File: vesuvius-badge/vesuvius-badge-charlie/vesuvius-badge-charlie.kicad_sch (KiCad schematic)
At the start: 9 parts, among them U1 IS31FL3731-QF, U2 Pico

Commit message: letters and vesuvius
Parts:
- added D1, D10, D100, D101, D102, D103, D104, D105, D106, D107, D108, D109, D11, D110, D111, D112, D113, D114, D115, D116, D117, D118, D119, D12, D120, D121, D122, D123, D124, D125, D126, D127, D128, D129, D13, D130, D131, D132, D133, D134, D135, D136, D137, D138, D139, D14, D140, D141, D142, D143, D144, D15, D16, D17, D18, D19, D2, D20, D21, D22, D23, D24, D25, D26, D27, D28, D29, D3, D30, D31, D32, D33, D34, D35, D36, D37, D38, D39, D4, D40, D41, D42, D43, D44, D45, D46, D47, D48, D49, D5, D50, D51, D52, D53, D54, D55, D56, D57, D58, D59, D6, D60, D61, D62, D63, D64, D65, D66, D67, D68, D69, D7, D70, D71, D72, D73, D74, D75, D76, D77, D78, D79, D8, D80, D81, D82, D83, D84, D85, D86, D87, D88, D89, D9, D90, D91, D92, D93, D94, D95, D96, D97, D98, D99: LED, LED_SMD:LED_0402_1005Metric, symbol Device:LED
- C1, C2, C3: renamed from C?; footprint (none) -> Capacitor_SMD:C_0603_1608Metric
- R1, R2, R3, R4: renamed from R?; footprint (none) -> Resistor_SMD:R_0603_1608Metric
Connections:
- net CA9: now reaches U1.1 (CA9)
- net CA9: now also D104.2 (A), D120.2 (A), D129.1 (K), D130.1 (K), D131.1 (K), D132.1 (K), D133.1 (K), D134.1 (K), D135.1 (K), D136.1 (K), D24.2 (A), D40.2 (A), D56.2 (A), D72.2 (A), D8.2 (A), D88.2 (A)
- net CB4: now reaches U1.10 (CB4)
- net CB4: now also D108.2 (A), D11.2 (A), D124.2 (A), D140.2 (A), D27.2 (A), D43.2 (A), D57.1 (K), D58.1 (K), D59.1 (K), D60.1 (K), D61.1 (K), D62.1 (K), D63.1 (K), D64.1 (K), D76.2 (A), D92.2 (A)
- net CB5: now reaches U1.11 (CB5)
- net CB5: now also D109.2 (A), D12.2 (A), D125.2 (A), D141.2 (A), D28.2 (A), D44.2 (A), D60.2 (A), D73.1 (K), D74.1 (K), D75.1 (K), D76.1 (K), D77.1 (K), D78.1 (K), D79.1 (K), D80.1 (K), D93.2 (A)
- net CB6: now reaches U1.12 (CB6)
- net CB6: now also D110.2 (A), D126.2 (A), D13.2 (A), D142.2 (A), D29.2 (A), D45.2 (A), D61.2 (A), D77.2 (A), D89.1 (K), D90.1 (K), D91.1 (K), D92.1 (K), D93.1 (K), D94.1 (K), D95.1 (K), D96.1 (K)
- net CB7: now reaches U1.13 (CB7)
- net CB7: now also D105.1 (K), D106.1 (K), D107.1 (K), D108.1 (K), D109.1 (K), D110.1 (K), D111.1 (K), D112.1 (K), D127.2 (A), D14.2 (A), D143.2 (A), D30.2 (A), D46.2 (A), D62.2 (A), D78.2 (A), D94.2 (A)
- net CB8: now reaches U1.14 (CB8)
- net CB8: now also D111.2 (A), D121.1 (K), D122.1 (K), D123.1 (K), D124.1 (K), D125.1 (K), D126.1 (K), D127.1 (K), D128.1 (K), D144.2 (A), D15.2 (A), D31.2 (A), D47.2 (A), D63.2 (A), D79.2 (A), D95.2 (A)
- net CB9: now reaches U1.15 (CB9)
- net CB9: now also D112.2 (A), D128.2 (A), D137.1 (K), D138.1 (K), D139.1 (K), D140.1 (K), D141.1 (K), D142.1 (K), D143.1 (K), D144.1 (K), D16.2 (A), D32.2 (A), D48.2 (A), D64.2 (A), D80.2 (A), D96.2 (A)
- net CA1: now reaches U1.21 (CA1)
- net CA1: now also D1.1 (K), D113.2 (A), D129.2 (A), D17.2 (A), D2.1 (K), D3.1 (K), D33.2 (A), D4.1 (K), D49.2 (A), D5.1 (K), D6.1 (K), D65.2 (A), D7.1 (K), D8.1 (K), D81.2 (A), D97.2 (A)
- net CA2: now reaches U1.22 (CA2)
- net CA2: now also D1.2 (A), D114.2 (A), D130.2 (A), D17.1 (K), D18.1 (K), D19.1 (K), D20.1 (K), D21.1 (K), D22.1 (K), D23.1 (K), D24.1 (K), D34.2 (A), D50.2 (A), D66.2 (A), D82.2 (A), D98.2 (A)
- net CA3: now reaches U1.23 (CA3)
- net CA3: now also D115.2 (A), D131.2 (A), D18.2 (A), D2.2 (A), D33.1 (K), D34.1 (K), D35.1 (K), D36.1 (K), D37.1 (K), D38.1 (K), D39.1 (K), D40.1 (K), D51.2 (A), D67.2 (A), D83.2 (A), D99.2 (A)
- net CA4: now reaches U1.24 (CA4)
- net CA4: now also D100.2 (A), D116.2 (A), D132.2 (A), D19.2 (A), D3.2 (A), D35.2 (A), D49.1 (K), D50.1 (K), D51.1 (K), D52.1 (K), D53.1 (K), D54.1 (K), D55.1 (K), D56.1 (K), D68.2 (A), D84.2 (A)
- net CA5: now reaches U1.25 (CA5)
- net CA5: now also D101.2 (A), D117.2 (A), D133.2 (A), D20.2 (A), D36.2 (A), D4.2 (A), D52.2 (A), D65.1 (K), D66.1 (K), D67.1 (K), D68.1 (K), D69.1 (K), D70.1 (K), D71.1 (K), D72.1 (K), D85.2 (A)
- net CA6: now reaches U1.26 (CA6)
- net CA6: now also D102.2 (A), D118.2 (A), D134.2 (A), D21.2 (A), D37.2 (A), D5.2 (A), D53.2 (A), D69.2 (A), D81.1 (K), D82.1 (K), D83.1 (K), D84.1 (K), D85.1 (K), D86.1 (K), D87.1 (K), D88.1 (K)
- net CA7: now reaches U1.27 (CA7)
- net CA7: now also D100.1 (K), D101.1 (K), D102.1 (K), D103.1 (K), D104.1 (K), D119.2 (A), D135.2 (A), D22.2 (A), D38.2 (A), D54.2 (A), D6.2 (A), D70.2 (A), D86.2 (A), D97.1 (K), D98.1 (K), D99.1 (K)
- net CA8: now reaches U1.28 (CA8)
- net CA8: now also D103.2 (A), D113.1 (K), D114.1 (K), D115.1 (K), D116.1 (K), D117.1 (K), D118.1 (K), D119.1 (K), D120.1 (K), D136.2 (A), D23.2 (A), D39.2 (A), D55.2 (A), D7.2 (A), D71.2 (A), D87.2 (A)
- net CB1: now reaches U1.7 (CB1)
- net CB1: now also D10.1 (K), D105.2 (A), D11.1 (K), D12.1 (K), D121.2 (A), D13.1 (K), D137.2 (A), D14.1 (K), D15.1 (K), D16.1 (K), D25.2 (A), D41.2 (A), D57.2 (A), D73.2 (A), D89.2 (A), D9.1 (K)
- net CB2: now reaches U1.8 (CB2)
- net CB2: now also D106.2 (A), D122.2 (A), D138.2 (A), D25.1 (K), D26.1 (K), D27.1 (K), D28.1 (K), D29.1 (K), D30.1 (K), D31.1 (K), D32.1 (K), D42.2 (A), D58.2 (A), D74.2 (A), D9.2 (A), D90.2 (A)
- net CB3: now reaches U1.9 (CB3)
- net CB3: now also D10.2 (A), D107.2 (A), D123.2 (A), D139.2 (A), D26.2 (A), D41.1 (K), D42.1 (K), D43.1 (K), D44.1 (K), D45.1 (K), D46.1 (K), D47.1 (K), D48.1 (K), D59.2 (A), D75.2 (A), D91.2 (A)
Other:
- moved on the sheet: C1, C2, C3, R1, R2, R3, R4, U1, U2

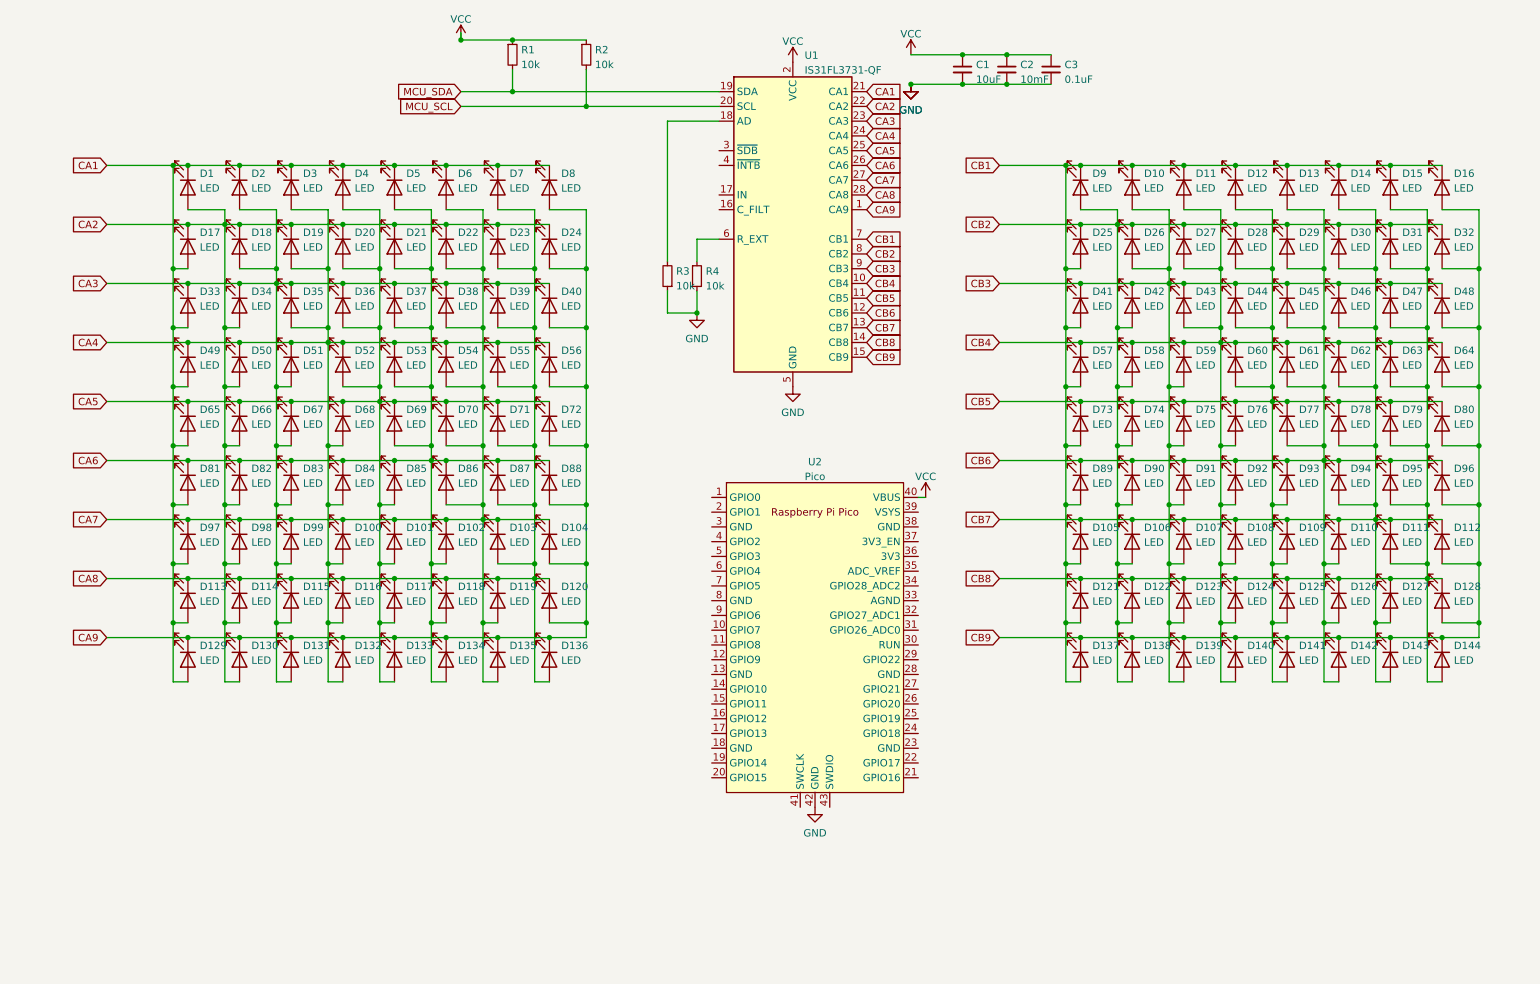
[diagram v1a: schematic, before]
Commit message: letters done, now the rest of the wiring
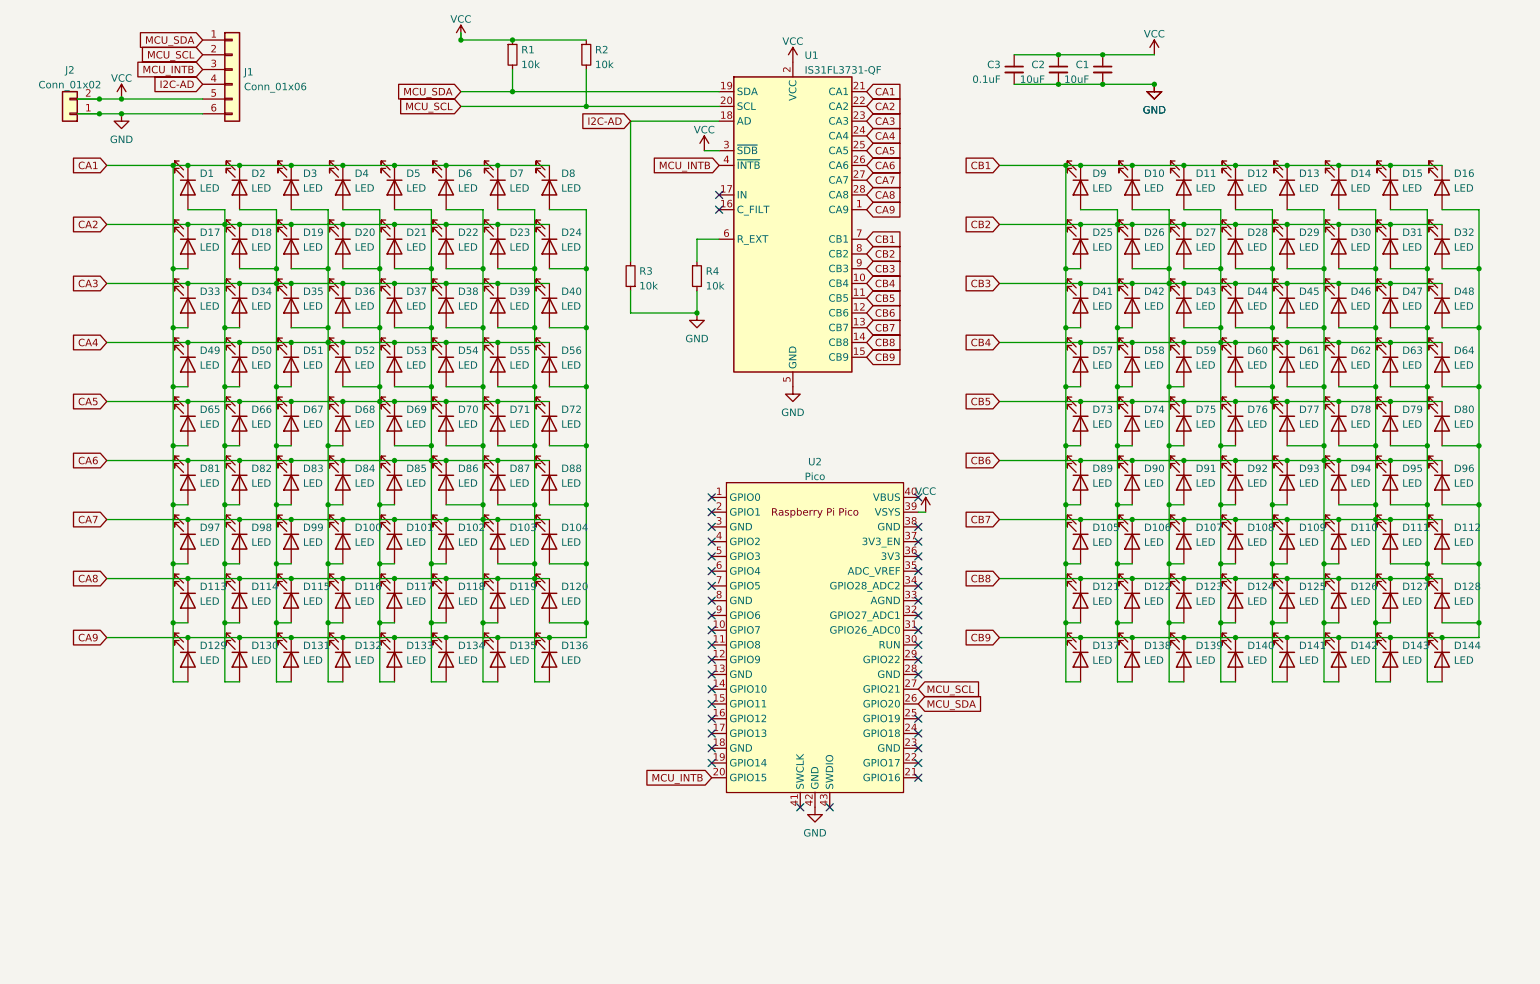
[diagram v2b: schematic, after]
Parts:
- added J1: Conn_01x06, Connector_PinHeader_2.54mm:PinHeader_1x06_P2.54mm_Horizontal, symbol Connector_Generic:Conn_01x06
- added J2: Conn_01x02, Connector_PinHeader_2.54mm:PinHeader_1x02_P2.54mm_Horizontal, symbol Connector_Generic:Conn_01x02
- C1, C3: footprint Capacitor_SMD:C_0603_1608Metric -> Capacitor_SMD:C_0402_1005Metric
- C2: value 10mF -> 10uF; footprint Capacitor_SMD:C_0603_1608Metric -> Capacitor_SMD:C_0402_1005Metric
- U2: footprint MCU_RaspberryPi_and_Boards:RPi_Pico_SMD_TH -> MCU_RaspberryPi_and_Boards:RPi_Pico_SMD
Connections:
- net GND: now also J1.6 (Pin_6), J2.1 (Pin_1)
- net MCU_SCL: now also U2.27 (GPIO21), J1.2 (Pin_2)
- net MCU_SDA: now also U2.26 (GPIO20), J1.1 (Pin_1)
- net VCC: now also U1.3 (~{SDB}), U2.39 (VSYS), J1.5 (Pin_5), J2.2 (Pin_2); no longer U2.40 (VBUS)
- net I2C-AD: now reaches R3.2, U1.18 (AD)
- net I2C-AD: now also J1.4 (Pin_4)
- net MCU_INTB: now reaches U1.4 (~{INTB})
- net MCU_INTB: now also U2.20 (GPIO15), J1.3 (Pin_3)
- no-connect marks 0 -> 40
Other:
- moved on the sheet: C1, C2, C3, R3

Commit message: wiring done
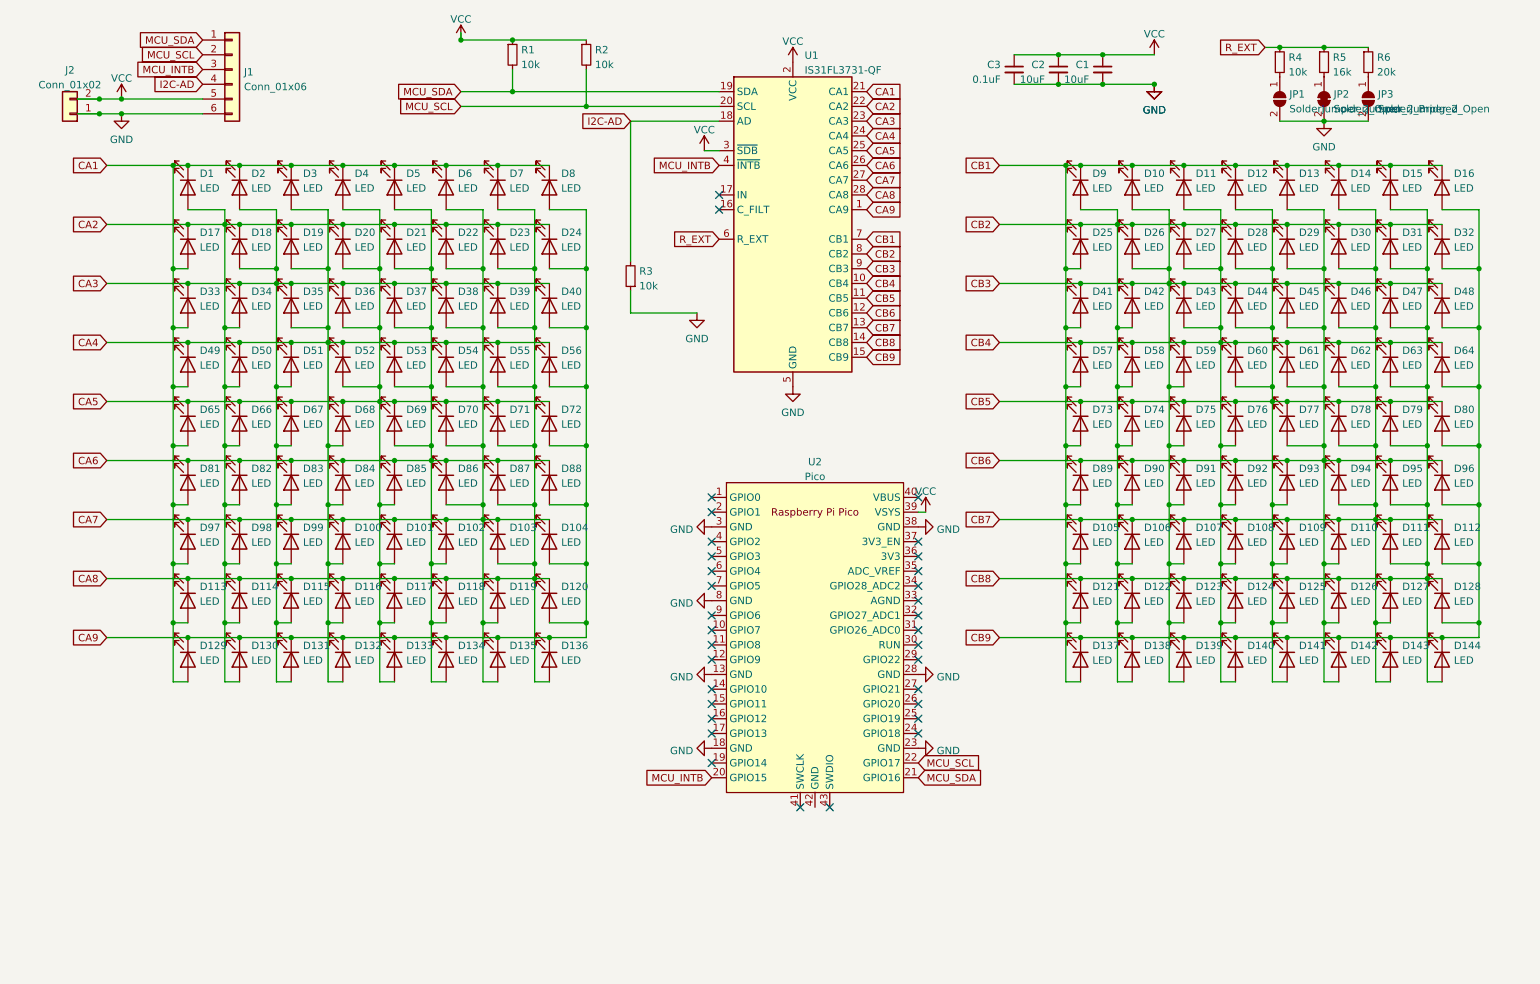
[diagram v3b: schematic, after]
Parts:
- added JP1, JP3: SolderJumper_2_Open, Jumper:SolderJumper-2_P1.3mm_Open_Pad1.0x1.5mm, symbol Jumper:SolderJumper_2_Open
- added JP2: SolderJumper_2_Bridged, Jumper:SolderJumper-2_P1.3mm_Bridged_Pad1.0x1.5mm, symbol Jumper:SolderJumper_2_Bridged
- added R5: 16k, Resistor_SMD:R_0603_1608Metric, symbol Device:R_Small
- added R6: 20k, Resistor_SMD:R_0603_1608Metric, symbol Device:R_Small
- J1: footprint Connector_PinHeader_2.54mm:PinHeader_1x06_P2.54mm_Horizontal -> Connector_PinHeader_2.54mm:PinHeader_1x06_P2.54mm_Vertical
- J2: footprint Connector_PinHeader_2.54mm:PinHeader_1x02_P2.54mm_Horizontal -> Connector_PinHeader_2.54mm:PinHeader_1x02_P2.54mm_Vertical
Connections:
- net GND: now also U2.13 (GND), U2.18 (GND), U2.23 (GND), U2.28 (GND), U2.3 (GND), U2.38 (GND), U2.8 (GND), JP1.2 (B), JP2.2 (B), JP3.2 (B); no longer R4.2, U2.42 (GND)
- net MCU_SCL: now also U2.22 (GPIO17); no longer U2.27 (GPIO21)
- net MCU_SDA: now also U2.21 (GPIO16); no longer U2.26 (GPIO20)
- net R_EXT: now reaches R4.1, U1.6 (R_EXT)
- net R_EXT: now also R5.1, R6.1
- new net: JP3.1 (A), R6.2
- new net: JP1.1 (A), R4.2
- new net: JP2.1 (A), R5.2
- no-connect marks 40 -> 33
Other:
- moved on the sheet: R4

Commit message: before applying purple diode footprint resize
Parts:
- removed J1: Conn_01x06, Connector_PinHeader_2.54mm:PinHeader_1x06_P2.54mm_Vertical, symbol Connector_Generic:Conn_01x06
- added 11: CH32V003J4M6, Package_SO:SOP-8_3.9x4.9mm_P1.27mm, symbol wch-mcu:CH32V003J4M6
- added H1, H2: MountingHole, MountingHole:MountingHole_5.3mm_M5, symbol Mechanical:MountingHole
- added J1: Conn_01x07, Connector_PinHeader_2.54mm:PinHeader_1x07_P2.54mm_Vertical, symbol Connector_Generic:Conn_01x07
- D10, D107, D115, D13, D19, D38, D43, D52, D65, D88: footprint LED_SMD:LED_0402_1005Metric -> LED_SMD:LED_0603_1608Metric
- R5: value 16k -> 15k
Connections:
- net GND: now also 11.2 (VSS), J1.7 (Pin_7)
- net I2C-AD: now also J1.5 (Pin_5)
- net MCU_INTB: now also 11.1 (PA1/PD6), J1.4 (Pin_4)
- net MCU_SCL: now also 11.6 (PC2), J1.3 (Pin_3)
- net MCU_SDA: now also 11.5 (PC1), J1.2 (Pin_2)
- net VCC: now also 11.4 (VDD), J1.6 (Pin_6)
- new net CH32V003_SWIO: 11.8 (PD1/PD4/PD5), J1.1 (Pin_1)
- no-connect marks 33 -> 35
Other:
- moved on the sheet: J2

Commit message: finished functional parts
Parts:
- removed J1: Conn_01x07, Connector_PinHeader_2.54mm:PinHeader_1x07_P2.54mm_Vertical, symbol Connector_Generic:Conn_01x07
- added J1: Conn_01x06, Connector_PinHeader_2.54mm:PinHeader_1x06_P2.54mm_Vertical, symbol Connector_Generic:Conn_01x06
- added JP4: SolderJumper_2_Open, Jumper:SolderJumper-2_P1.3mm_Open_Pad1.0x1.5mm, symbol Jumper:SolderJumper_2_Open
- R1, R2: value 10k -> 4k7
- renumbered 11 to 11111
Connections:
- net CH32V003_SWIO: now also J1.1 (Pin_1)
- net I2C-AD: now also J1.5 (Pin_5)
- net MCU_INTB: now also J1.4 (Pin_4)
- net MCU_SCL: now also J1.3 (Pin_3)
- net MCU_SDA: now also J1.2 (Pin_2)
- net VCC: now also U2.36 (3V3), J1.6 (Pin_6), JP4.2 (B); no longer J2.2 (Pin_2), U2.39 (VSYS)
- new net +BATT: J2.2 (Pin_2), JP4.1 (A), U2.39 (VSYS)
- no-connect marks 35 -> 34
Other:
- moved on the sheet: J2

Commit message: final files and gerbers as submitted to production
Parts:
- removed J1: Conn_01x06, Connector_PinHeader_2.54mm:PinHeader_1x06_P2.54mm_Vertical, symbol Connector_Generic:Conn_01x06
- removed J2: Conn_01x02, Connector_PinHeader_2.54mm:PinHeader_1x02_P2.54mm_Vertical, symbol Connector_Generic:Conn_01x02
- added F1: Fuse_Small, Fuse:Fuse_0402_1005Metric, symbol Device:Fuse_Small
- added J1: Conn_01x05, Connector_PinHeader_2.54mm:PinHeader_1x05_P2.54mm_Vertical, symbol Connector_Generic:Conn_01x05
- added J2: Conn_01x03, Connector_PinHeader_2.54mm:PinHeader_1x03_P2.54mm_Vertical, symbol Connector_Generic:Conn_01x03
- C1, C2: LCSC (none) -> C15525
- C3: value 0.1uF -> 100nF; LCSC (none) -> C1525
- D1, D100, D101, D102, D103, D104, D105, D106, D108, D109, D11, D110, D111, D112, D113, D114, D116, D117, D118, D119, D12, D120, D121, D122, D123, D124, D125, D126, D127, D129, D130, D131, D132, D133, D134, D135, D136, D137, D138, D139, D140, D141, D143, D144, D15, D17, D18, D2, D20, D21, D22, D24, D25, D26, D27, D28, D29, D3, D31, D33, D34, D35, D36, D37, D4, D40, D41, D42, D44, D45, D47, D49, D5, D50, D51, D53, D54, D55, D56, D57, D58, D59, D6, D60, D61, D62, D63, D64, D66, D67, D68, D69, D70, D71, D72, D73, D74, D75, D76, D77, D79, D8, D81, D82, D83, D84, D85, D86, D87, D89, D9, D90, D91, D92, D93, D94, D95, D96, D97, D98, D99: value LED -> LED white; LCSC (none) -> C965796
- D10, D107, D115, D13, D19, D38, D43, D52, D65, D88: value LED -> LED purple; LCSC (none) -> C7371898
- D128, D30, D39, D46, D78: value LED -> LED orange; LCSC (none) -> C779448
- D14, D142, D16, D23, D32, D48, D7, D80: value LED -> LED red; LCSC (none) -> C779449
- R1, R2: LCSC (none) -> C23162
- R3, R4: LCSC (none) -> C25804
- R5: LCSC (none) -> C22809
- R6: LCSC (none) -> C4184
- U1: LCSC (none) -> C191206
- renumbered 11111 to U3
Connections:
- net +BATT: now also F1.2
- net CH32V003_SWIO: now also J2.1 (Pin_1)
- net GND: now also J2.2 (Pin_2)
- net I2C-AD: now also J1.4 (Pin_4)
- net MCU_INTB: now also J1.3 (Pin_3)
- net MCU_SCL: now also J1.2 (Pin_2)
- net MCU_SDA: now also J1.1 (Pin_1)
- net VCC: now also J1.5 (Pin_5)
- new net: F1.1, J2.3 (Pin_3)
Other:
- moved on the sheet: R2
